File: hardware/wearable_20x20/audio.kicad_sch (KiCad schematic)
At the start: 15 parts, among them U30 TLV9001IDCKR

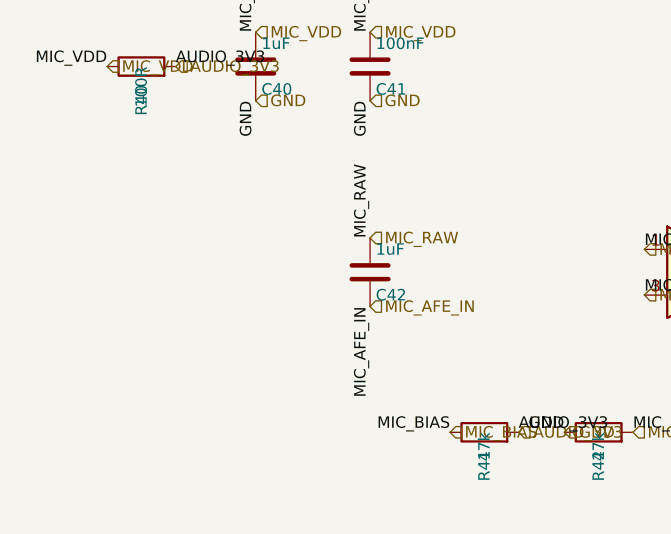
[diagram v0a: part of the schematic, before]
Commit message: Regenerate hierarchies with selected EVT parts
Co-authored-by: illiapliukhin <illiapliukhin@users.noreply.github.com>
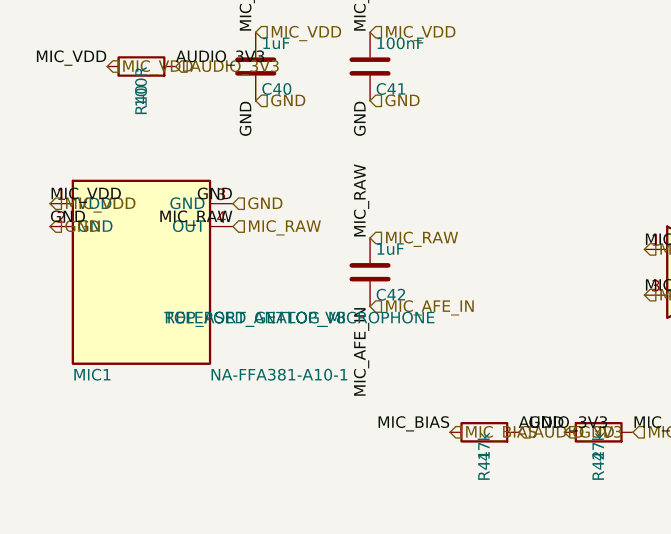
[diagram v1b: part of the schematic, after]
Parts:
- added MIC1: NA-FFA381-A10-1, PartSignal_Packages:Gettop_NA-FFA381-A10-1_TopPort_Microphone, symbol PartSignal_Platform:NA-FFA381-A10-1
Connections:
- net GND: now also MIC1.2 (GND), MIC1.3 (GND)
- net MIC_RAW: now also MIC1.4 (OUT)
- net MIC_VDD: now also MIC1.1 (VDD)
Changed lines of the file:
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@@
+		)
+	)
+	(label "GND"
+		(at 20.32 55.88 0)
+		(effects
+			(font
+				(size 1.27 1.27)
+			)
+			(justify left bottom)
 		)
 	)
@@
 		)
 	)
+	(label "GND"
+		(at 40.64 53.34 180)
+		(effects
+			(font
+				(size 1.27 1.27)
+			)
+			(justify right bottom)
+		)
+	)
 	(label "MIC_AFE_OUT"
 		(at 161.29 60.96 0)
@@
 		)
 	)
+	(label "MIC_VDD"
+		(at 20.32 53.34 0)
+		(effects
+			(font
+				(size 1.27 1.27)
+			)
+			(justify left bottom)
+		)
+	)
+	(label "MIC_RAW"
+		(at 40.64 55.88 180)
+		(effects
+			(font
+				(size 1.27 1.27)
+			)
+			(justify right bottom)
+		)
+	)
 	(label "MIC_AFE_FB"
 		(at 101.6 60.96 180)
@@
 	(hierarchical_label "GND"
 		(shape input)
+		(at 20.32 55.88 0)
+		(effects
+			(font
+				(size 1.27 1.27)
+			)
+			(justify left)
+		)
+	)
+	(hierarchical_label "GND"
+		(shape input)
 		(at 172.72 80.01 0)
 		(effects
@@
 	(hierarchical_label "GND"
 		(shape input)
+		(at 40.64 53.34 0)
+		(effects
+			(font
+				(size 1.27 1.27)
+			)
+			(justify left)
+		)
+	)
+	(hierarchical_label "MIC_RAW"
+		(shape input)
+		(at 40.64 55.88 0)
+		(effects
+			(font
+				(size 1.27 1.27)
+			)
+			(justify left)
+		)
+	)
+	(hierarchical_label "GND"
+		(shape input)
 		(at 93.98 82.55 0)
 		(effects
@@
 		(shape input)
 		(at 153.67 60.96 0)
+		(effects
+			(font
+				(size 1.27 1.27)
+			)
+			(justify left)
+		)
+	)
+	(hierarchical_label "MIC_VDD"
+		(shape input)
+		(at 20.32 53.34 0)
 		(effects
 			(font
@@
 					(unit 1)
 				)
+			)
+		)
+	)
+	(symbol
+		(lib_id "PartSignal_Platform:NA-FFA381-A10-1")
+		(at 30.48 60.96 0)
+		(unit 1)
+		(body_style 1)
+		(exclude_from_sim no)
+		(in_bom yes)
+		(on_board yes)
+		(in_pos_files yes)
+		(dnp no)
+		(property "Reference" "MIC1"
+			(at 22.86 72.39 0)
+			(show_name no)
+			(do_not_autoplace no)
+			(effects
+				(font
+					(size 1.27 1.27)
+				)
+				(justify left)
+			)
+		)
+		(property "Value" "NA-FFA381-A10-1"
+			(at 38.1 72.39 0)
+			(show_name no)
+			(do_not_autoplace no)
+			(effects
+				(font
+					(size 1.27 1.27)
+				)
+				(justify left)
+			)
+		)
+		(property "Footprint" "PartSignal_Packages:Gettop_NA-FFA381-A10-1_TopPort_Microphone"
+			(at 30.48 60.96 0)
+			(hide yes)
+			(show_name no)
+			(do_not_autoplace no)
+			(effects
+				(font
+					(size 1.27 1.27)
+				)
+			)
+		)
+		(property "Datasheet" ""
+			(at 30.48 60.96 0)
+			(show_name no)
+			(do_not_autoplace no)
+			(effects
+				(font
+					(size 1.27 1.27)
+				)
+			)
+		)
+		(property "Description" ""
+			(at 30.48 60.96 0)
+			(show_name no)
+			(do_not_autoplace no)
+			(effects
+				(font
+					(size 1.27 1.27)
+				)
+			)
+		)
+		(property "Function" "TOP_PORT_ANALOG_MICROPHONE"
+			(at 33.02 66.0399 0)
+			(show_name no)
+			(do_not_autoplace no)
+			(effects
+				(font
+					(size 1.27 1.27)
+				)
+				(justify left)
+			)
+		)
+		(property "FootprintStatus" "RELEASED_GETTOP_V8"
+			(at 33.02 66.0399 0)
+			(show_name no)
+			(do_not_autoplace no)
+			(effects
+				(font
+					(size 1.27 1.27)
+				)
+				(justify left)
+			)
+		)
+		(pin "1"
+		)
+		(pin "2"
+		)
+		(pin "3"
+		)
+		(pin "4"
+		)
+		(instances
+			(project ""
+				(path "/cee8a5eb-ba57-5bb9-9b24-255b95f07e0c"
+					(reference "MIC1")
+					(unit 1)
+				)
